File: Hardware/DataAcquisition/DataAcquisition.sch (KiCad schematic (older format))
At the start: 0 parts

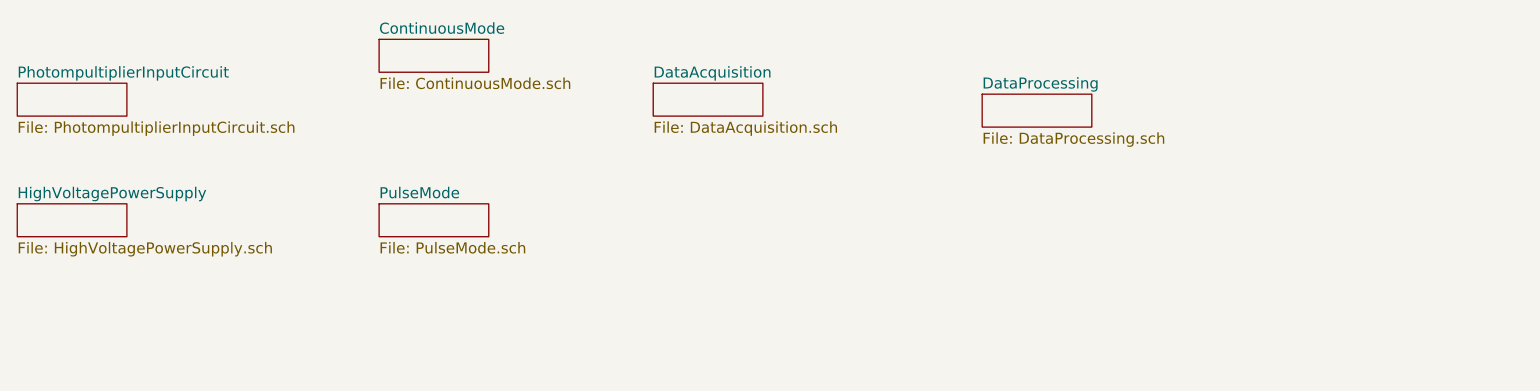
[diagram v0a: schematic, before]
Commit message: split (previousle one) pcb project to three separate pcbs
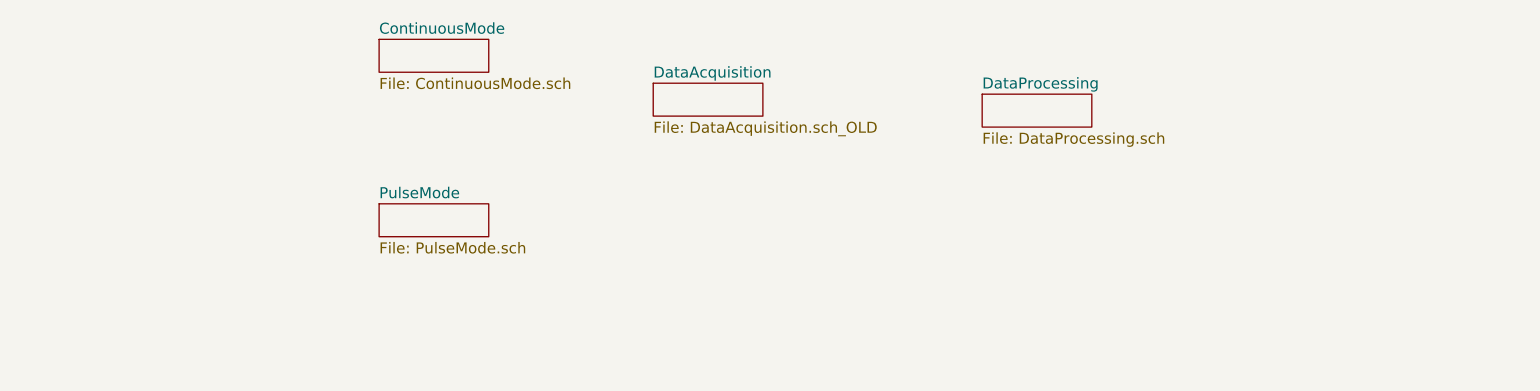
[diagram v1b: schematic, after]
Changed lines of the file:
@@
 $Descr A4 11693 8268
 encoding utf-8
-Sheet 1 7
+Sheet 1 5
 Title ""
 Date ""
@@
 U 5EDA53F3
 F0 "DataAcquisition" 50
-F1 "DataAcquisition.sch" 50
+F1 "DataAcquisition.sch_OLD" 50
 $EndSheet
 $Sheet
-S 900  2450 500  150
-U 5EDA5628
-F0 "HighVoltagePowerSupply" 50
-F1 "HighVoltagePowerSupply.sch" 50
-$EndSheet
-$Sheet
-S 900  1900 500  150
-U 5EDA585D
-F0 "PhotompultiplierInputCircuit" 50
-F1 "PhotompultiplierInputCircuit.sch" 50
-$EndSheet
-$Sheet

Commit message: Finished PCB for HV power supply, added correct PCB outlines for acquisition PCB.
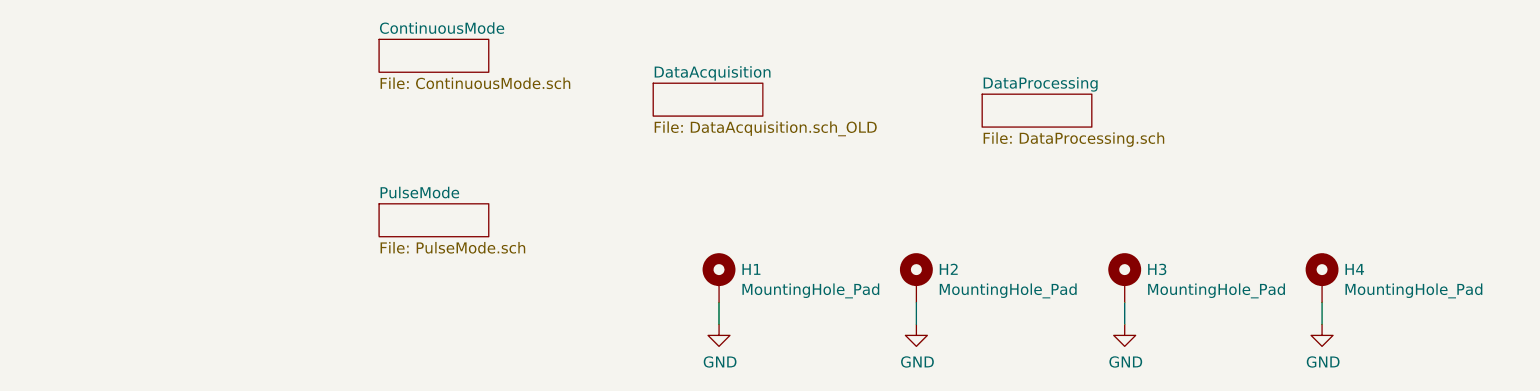
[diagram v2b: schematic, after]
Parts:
- added H1, H2, H3, H4: MountingHole_Pad, MountingHole:MountingHole_3.5mm_Pad, symbol Mechanical:MountingHole_Pad
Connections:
- new net GND: H1.1, H2.1, H3.1, H4.1
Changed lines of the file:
@@
 F1 "PulseMode.sch" 50
 $EndSheet
+$Comp
+L Mechanical:MountingHole_Pad H1
+U 1 1 5FAAC1D2
+P 4100 2800
+F 0 "H1" H 4200 2849 50  0000 L CNN
+F 1 "MountingHole_Pad" H 4200 2758 50  0000 L CNN
+F 2 "MountingHole:MountingHole_3.5mm_Pad" H 4100 2800 50  0001 C CNN
+F 3 "~" H 4100 2800 50  0001 C CNN
+	1    4100 2800
+	1    0    0    -1
+$EndComp
+$Comp
+L power:GND #PWR055
+U 1 1 5FAAC4A0
+P 4100 3000
+F 0 "#PWR055" H 4100 2750 50  0001 C CNN
+F 1 "GND" H 4105 2827 50  0000 C CNN
+F 2 "" H 4100 3000 50  0001 C CNN
+F 3 "" H 4100 3000 50  0001 C CNN
+	1    4100 3000
+	1    0    0    -1
+$EndComp
+Wire Wire Line
+	4100 2900 4100 3000
+$Comp
+L Mechanical:MountingHole_Pad H2
+U 1 1 5FAAD33C
+P 5000 2800
+F 0 "H2" H 5100 2849 50  0000 L CNN
+F 1 "MountingHole_Pad" H 5100 2758 50  0000 L CNN
+F 2 "MountingHole:MountingHole_3.5mm_Pad" H 5000 2800 50  0001 C CNN
+F 3 "~" H 5000 2800 50  0001 C CNN
+	1    5000 2800
+	1    0    0    -1
+$EndComp
+$Comp
+L power:GND #PWR056
+U 1 1 5FAAD342
+P 5000 3000
+F 0 "#PWR056" H 5000 2750 50  0001 C CNN
+F 1 "GND" H 5005 2827 50  0000 C CNN
+F 2 "" H 5000 3000 50  0001 C CNN
+F 3 "" H 5000 3000 50  0001 C CNN
+	1    5000 3000
+	1    0    0    -1
+$EndComp
+Wire Wire Line
+	5000 2900 5000 3000
+$Comp
+L Mechanical:MountingHole_Pad H3
+U 1 1 5FAAE307
+P 5950 2800
+F 0 "H3" H 6050 2849 50  0000 L CNN
+F 1 "MountingHole_Pad" H 6050 2758 50  0000 L CNN
+F 2 "MountingHole:MountingHole_3.5mm_Pad" H 5950 2800 50  0001 C CNN
+F 3 "~" H 5950 2800 50  0001 C CNN
+	1    5950 2800
+	1    0    0    -1
+$EndComp
+$Comp
+L power:GND #PWR057
+U 1 1 5FAAE30D
+P 5950 3000
+F 0 "#PWR057" H 5950 2750 50  0001 C CNN
+F 1 "GND" H 5955 2827 50  0000 C CNN
+F 2 "" H 5950 3000 50  0001 C CNN
+F 3 "" H 5950 3000 50  0001 C CNN
+	1    5950 3000
+	1    0    0    -1
+$EndComp
+Wire Wire Line
+	5950 2900 5950 3000
+$Comp
+L Mechanical:MountingHole_Pad H4
+U 1 1 5FAAE314
+P 6850 2800
+F 0 "H4" H 6950 2849 50  0000 L CNN
+F 1 "MountingHole_Pad" H 6950 2758 50  0000 L CNN
+F 2 "MountingHole:MountingHole_3.5mm_Pad" H 6850 2800 50  0001 C CNN
+F 3 "~" H 6850 2800 50  0001 C CNN
+	1    6850 2800
+	1    0    0    -1
+$EndComp
+$Comp
+L power:GND #PWR058
+U 1 1 5FAAE31A
+P 6850 3000
+F 0 "#PWR058" H 6850 2750 50  0001 C CNN
+F 1 "GND" H 6855 2827 50  0000 C CNN
+F 2 "" H 6850 3000 50  0001 C CNN
+F 3 "" H 6850 3000 50  0001 C CNN
+	1    6850 3000
+	1    0    0    -1
+$EndComp
+Wire Wire Line
+	6850 2900 6850 3000
 $EndSCHEMATC

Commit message: Clarify architecture of acquisition module (#80), removed obsolete files
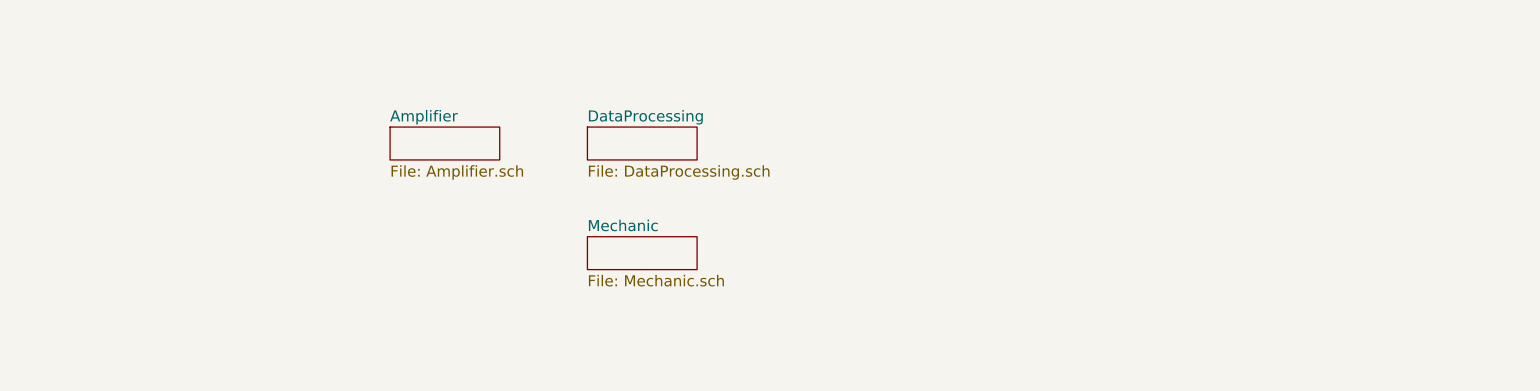
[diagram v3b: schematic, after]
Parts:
- removed H1, H2, H3, H4: MountingHole_Pad, MountingHole:MountingHole_3.5mm_Pad, symbol Mechanical:MountingHole_Pad
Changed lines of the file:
@@
 $Descr A4 11693 8268
 encoding utf-8
-Sheet 1 5
+Sheet 1 3
 Title ""
 Date ""
@@
 $EndDescr
 $Sheet
-S 3800 1900 500  150
-U 5EDA53F3
-F0 "DataAcquisition" 50
-F1 "DataAcquisition.sch_OLD" 50
+S 2600 2100 500  150
+U 5FABF6F9
+F0 "Amplifier" 50
+F1 "Amplifier.sch" 50
 $EndSheet
 $Sheet
-S 5300 1950 500  150
-U 5EF1F288
+S 3500 2100 500  150
+U 5FABF848
 F0 "DataProcessing" 50
 F1 "DataProcessing.sch" 50
 $EndSheet
 $Sheet
-S 2550 1700 500  150
-U 5EE61922
-F0 "ContinuousMode" 50
-F1 "ContinuousMode.sch" 50
+S 3500 2600 500  150
+U 5FAC655A
+F0 "Mechanic" 50
+F1 "Mechanic.sch" 50
 $EndSheet
-$Sheet
-S 2550 2450 500  150
-U 5EE9D63B
-F0 "PulseMode" 50
-F1 "PulseMode.sch" 50
-$EndSheet
-$Comp
-L Mechanical:MountingHole_Pad H1
-U 1 1 5FAAC1D2
-P 4100 2800
-F 0 "H1" H 4200 2849 50  0000 L CNN
-F 1 "MountingHole_Pad" H 4200 2758 50  0000 L CNN
-F 2 "MountingHole:MountingHole_3.5mm_Pad" H 4100 2800 50  0001 C CNN
-F 3 "~" H 4100 2800 50  0001 C CNN
-	1    4100 2800
-	1    0    0    -1
-$EndComp
-$Comp
-L power:GND #PWR055
-U 1 1 5FAAC4A0
-P 4100 3000
-F 0 "#PWR055" H 4100 2750 50  0001 C CNN
-F 1 "GND" H 4105 2827 50  0000 C CNN
-F 2 "" H 4100 3000 50  0001 C CNN
-F 3 "" H 4100 3000 50  0001 C CNN
-	1    4100 3000
-	1    0    0    -1
-$EndComp
-Wire Wire Line
-	4100 2900 4100 3000
-$Comp
-L Mechanical:MountingHole_Pad H2
-U 1 1 5FAAD33C
-P 5000 2800
-F 0 "H2" H 5100 2849 50  0000 L CNN
-F 1 "MountingHole_Pad" H 5100 2758 50  0000 L CNN
-F 2 "MountingHole:MountingHole_3.5mm_Pad" H 5000 2800 50  0001 C CNN
-F 3 "~" H 5000 2800 50  0001 C CNN
-	1    5000 2800
-	1    0    0    -1
-$EndComp
-$Comp
-L power:GND #PWR056
-U 1 1 5FAAD342
-P 5000 3000
-F 0 "#PWR056" H 5000 2750 50  0001 C CNN
-F 1 "GND" H 5005 2827 50  0000 C CNN
-F 2 "" H 5000 3000 50  0001 C CNN
-F 3 "" H 5000 3000 50  0001 C CNN
-	1    5000 3000
-	1    0    0    -1
-$EndComp
-Wire Wire Line
-	5000 2900 5000 3000
-$Comp
-L Mechanical:MountingHole_Pad H3
-U 1 1 5FAAE307
-P 5950 2800
-F 0 "H3" H 6050 2849 50  0000 L CNN
-F 1 "MountingHole_Pad" H 6050 2758 50  0000 L CNN
-F 2 "MountingHole:MountingHole_3.5mm_Pad" H 5950 2800 50  0001 C CNN
-F 3 "~" H 5950 2800 50  0001 C CNN
-	1    5950 2800
-	1    0    0    -1
-$EndComp
-$Comp
-L power:GND #PWR057
-U 1 1 5FAAE30D
-P 5950 3000
-F 0 "#PWR057" H 5950 2750 50  0001 C CNN
-F 1 "GND" H 5955 2827 50  0000 C CNN
-F 2 "" H 5950 3000 50  0001 C CNN
-F 3 "" H 5950 3000 50  0001 C CNN
-	1    5950 3000
-	1    0    0    -1
-$EndComp
-Wire Wire Line
-	5950 2900 5950 3000
-$Comp
-L Mechanical:MountingHole_Pad H4
-U 1 1 5FAAE314
-P 6850 2800
-F 0 "H4" H 6950 2849 50  0000 L CNN
-F 1 "MountingHole_Pad" H 6950 2758 50  0000 L CNN
-F 2 "MountingHole:MountingHole_3.5mm_Pad" H 6850 2800 50  0001 C CNN
-F 3 "~" H 6850 2800 50  0001 C CNN
-	1    6850 2800
-	1    0    0    -1
-$EndComp
-$Comp
-L power:GND #PWR058
-U 1 1 5FAAE31A
-P 6850 3000
-F 0 "#PWR058" H 6850 2750 50  0001 C CNN
-F 1 "GND" H 6855 2827 50  0000 C CNN
-F 2 "" H 6850 3000 50  0001 C CNN
-F 3 "" H 6850 3000 50  0001 C CNN
-	1    6850 3000
-	1    0    0    -1
-$EndComp
-Wire Wire Line
-	6850 2900 6850 3000
 $EndSCHEMATC
